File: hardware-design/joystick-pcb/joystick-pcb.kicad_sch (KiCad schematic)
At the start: 6 parts, among them J1 Wire_Pads, SW1 SKRHABE010

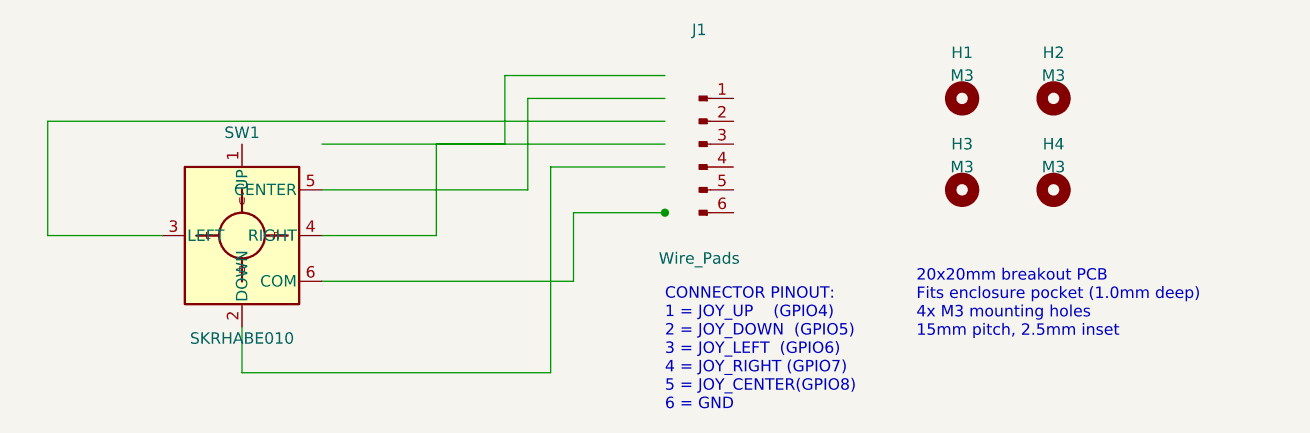
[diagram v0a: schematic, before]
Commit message: Joystick PCB Rev 2.0 — kleeb footprint, datasheet pinout, headless autoroute
Rev 1 of the joystick breakout shipped with three real bugs: a hand-drawn
SKRHABE010 footprint with the wrong pad geometry, a wire pad that
physically overlapped a mounting hole, and three pin assignments that
didn't match the Alps datasheet. Rev 2.0 fixes all three by cloning
proven references and adding machine-checkable verification.

PCB / schematic
- Footprint: cloned from crides/kleeb SKRHA-boss (production-tested in
  shipping keyboards), rotated -45° so pads land axis-aligned on the
  body's left/right faces. Includes the two NPTH alignment posts and
  two SMD anchor pads from the source.
- Pin names confirmed against the Alps SKRHABE010 datasheet circuit
  diagram (1=A, 2=Center, 3=C, 4=B, 5=Common, 6=D). Rev 1 had pins 2,
  5, and 6 wrong.
- Wire pads repositioned to bottom edge at 1.8mm pitch, 1.4mm OD /
  0.8mm drill. All clearances verified by Python script before drawing
  (0.74mm min pad↔hole, 1.0mm pad↔pad, 2.30mm to board edge).
- Schematic rebuilt from scratch using the kleeb symbol with proper
  pin names (A/Center/C/B/Common/D) and label-stub style routing.

Routing
- Autorouted headlessly via the official Freerouting Docker image
  (ghcr.io/freerouting/freerouting), with DSN export/SES import done
  through the pcbnew Python module. No GUI interaction required.
- 23 trace segments + 1 through-hole via, 534mm total length.
- 8 bends, all 45°. Zero 90° corners. 0 clearance violations.
- KiCad CLI DRC: 0 copper violations, 0 unconnected nets, 0 schematic
  parity issues.

Documentation
- New hardware-design/HARDWARE-DESIGN-PROCESS.md — retrospective on the
  SCAD→print and PCB→fab loops with concrete improvements to cut
  wasted prints (calibration coupons, SVG cross-sections, presets-
  instead-of-prints, mandatory dimension comment blocks).
- New hardware-design/scad Parts/README.md — documents the three
  Python helpers (scad-export.py, bake-preset.py, export-preset.py)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
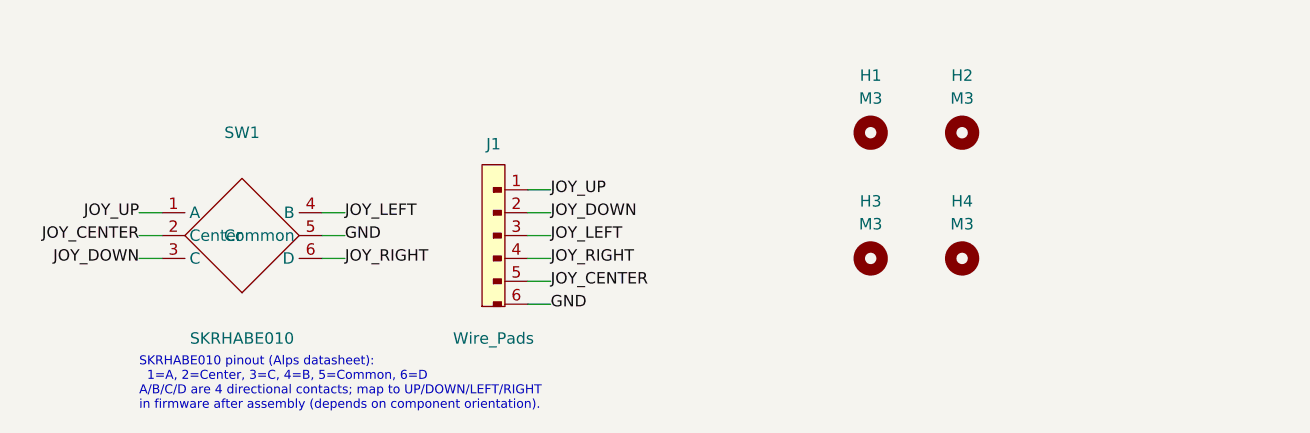
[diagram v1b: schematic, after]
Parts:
- J1: footprint joystick-pcb:WirePads_1x06_P2.0mm -> joystick-pcb:WirePads_1x06_P1.8mm
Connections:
- net JOY_UP: now reaches J1.1 (Pin_1)
- net JOY_UP: now also SW1.1 (A)
- net JOY_DOWN: now reaches J1.2 (Pin_2)
- net JOY_DOWN: now also SW1.3 (C)
- net JOY_LEFT: now reaches J1.3 (Pin_3)
- net JOY_LEFT: now also SW1.4 (B)
- net JOY_RIGHT: now reaches J1.4 (Pin_4)
- net JOY_RIGHT: now also SW1.6 (D)
- net JOY_CENTER: now reaches J1.5 (Pin_5)
- net JOY_CENTER: now also SW1.2 (Center)
- net GND: now reaches J1.6 (Pin_6)
- net GND: now also SW1.5 (Common)
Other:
- note added: "SKRHABE010 pinout (Alps datasheet): 1=A, 2=Center, 3=C, 4=B, 5=Common, 6=D A/B/C/D are 4 directional contacts; map to UP/DOWN/LEFT/RIGHT in firmware after assembly (depends on component orientation)."
- note removed: "20x20mm breakout PCB Fits enclosure pocket (1.0mm deep) 4x M3 mounting holes 15mm pitch, 2.5mm inset"
- note removed: "CONNECTOR PINOUT: 1 = JOY_UP (GPIO4) 2 = JOY_DOWN (GPIO5) 3 = JOY_LEFT (GPIO6) 4 = JOY_RIGHT (GPIO7) 5 = JOY_CENTER(GPIO8) 6 = GND"
